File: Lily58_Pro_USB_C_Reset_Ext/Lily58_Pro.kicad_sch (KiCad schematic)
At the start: 83 parts, among them J1 LED, J2 4PIN, J3 OLED, P1 i2c_pin, P2 i2c_pin, SW1 SW_PUSH, SW2 SW_PUSH, SW3 SW_PUSH, SW4 SW_PUSH, SW5 SW_PUSH, SW6 SW_PUSH, SW7 SW_PUSH, SW8 SW_PUSH, SW9 SW_PUSH, U1 ProMicro

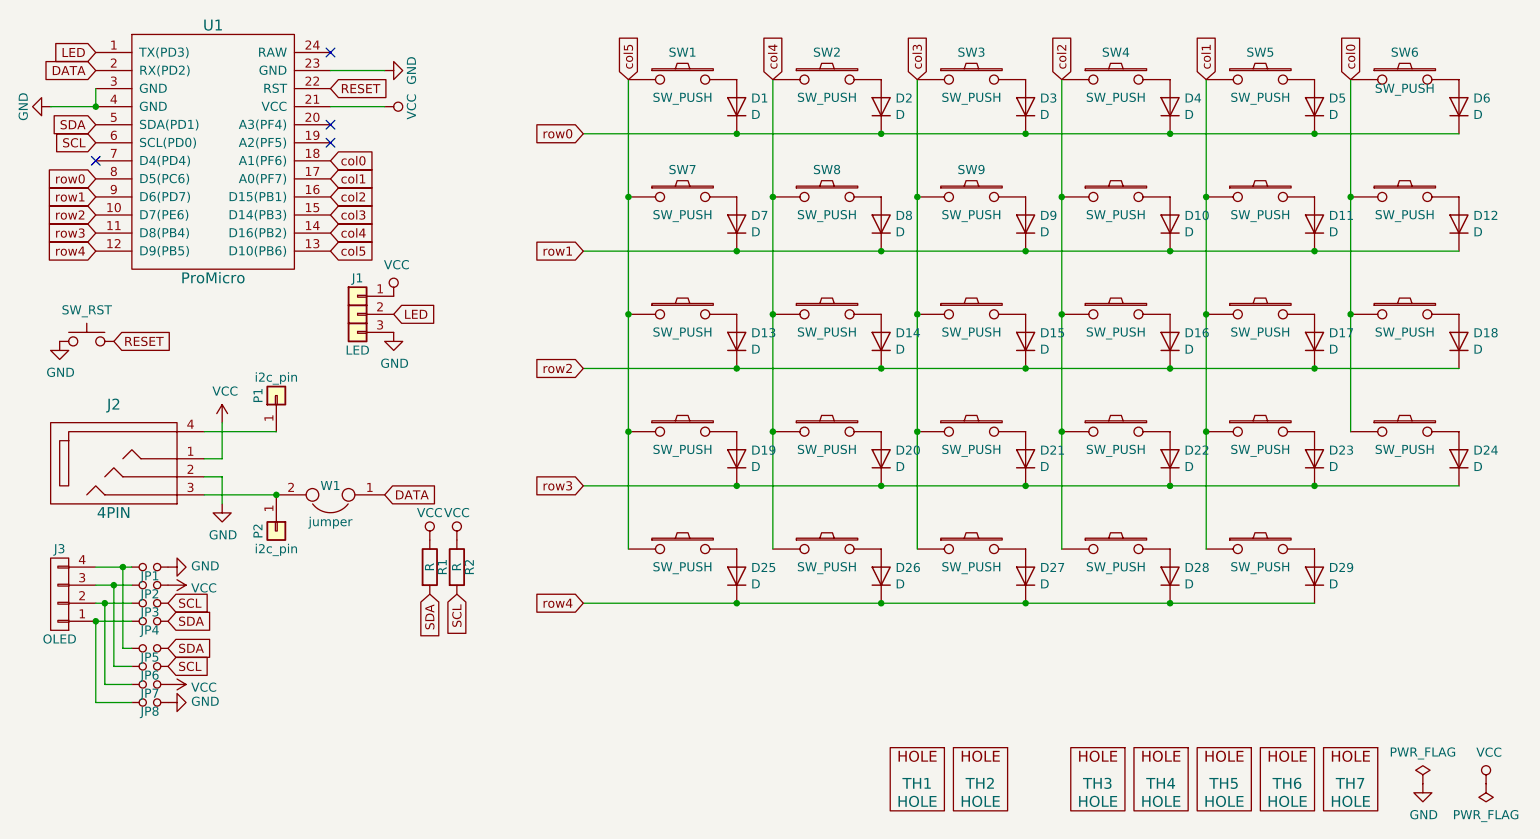
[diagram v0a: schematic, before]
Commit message: Lily58_Pro_USB_C_Reset_Ext: strip down
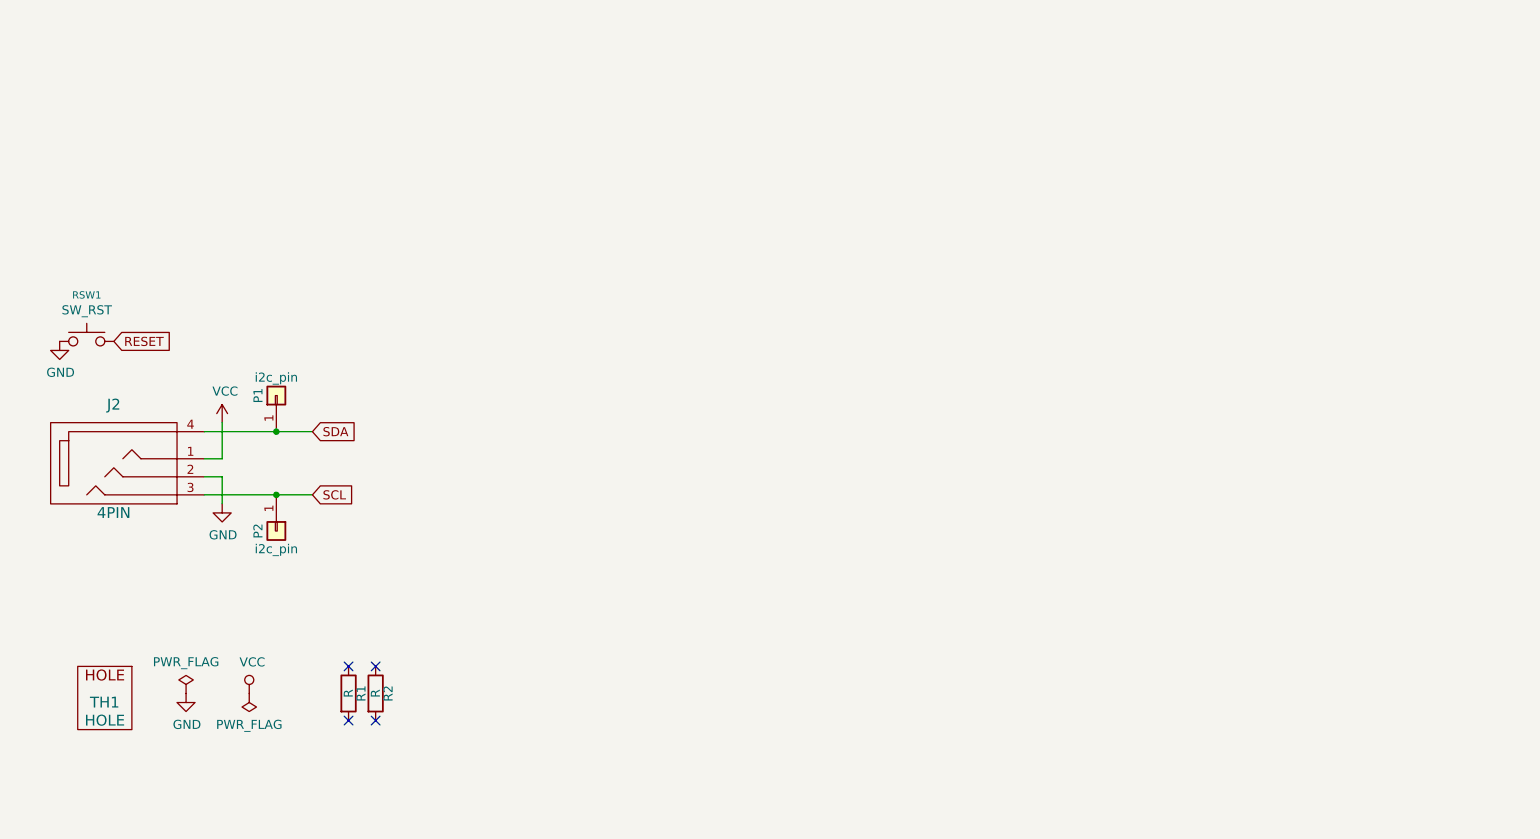
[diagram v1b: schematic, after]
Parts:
- removed ? (x20), SW1, SW2, SW3, SW4, SW5, SW6, SW7, SW8, SW9: SW_PUSH, Lily58-footprint:CherryMX_KailhLowProfile_Hotswap, symbol Lily58_Pro-rescue:SW_PUSH-Lily58-cache
- removed D1, D10, D11, D12, D13, D14, D15, D16, D17, D18, D19, D2, D20, D21, D22, D23, D24, D25, D26, D27, D28, D29, D3, D4, D5, D6, D7, D8, D9: D, Lily58-footprint:Diode_SOD123, symbol Lily58_Pro-rescue:D-Lily58-cache
- removed J1: LED, Lily58-footprint:LED, symbol Lily58_Pro-rescue:LED-Lily58-cache
- removed J3: OLED, Lily58-footprint:OLED_4Pin, symbol Lily58_Pro-rescue:OLED-Lily58-cache
- removed JP1, JP2, JP3, JP4, JP5, JP6, JP7, JP8: Jumper_NO_Small, Lily58-footprint:Jumper, symbol Lily58_Pro-rescue:Jumper_NO_Small-Device
- removed TH2: HOLE, Lily58-footprint:M2_HOLE_PCB, symbol Lily58_Pro-rescue:HOLE-Lily58-cache
- removed TH3, TH4, TH5, TH6, TH7: HOLE, Lily58-footprint:HOLE_M2_TH, symbol Lily58_Pro-rescue:HOLE-Lily58-cache
- removed U1: ProMicro, Lily58-footprint:ProMicro_rev2, symbol Lily58_Pro-rescue:ProMicro_2-Lily58-cache
- removed W1: jumper, Lily58-footprint:jumper_data, symbol Lily58_Pro-rescue:Jumper-Device
- gave numbers to parts that had none: 1
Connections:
- net SCL: now also J2.3, P2.1 (Pin_1); no longer R2.2
- net SDA: now also J2.4, P1.1 (Pin_1); no longer R1.2
- net VCC: no longer R1.1, R2.1
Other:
- moved on the sheet: R1, R2, TH1

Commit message: Lily58_Pro_USB_C_Reset_Ext: add usb and reset
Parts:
- added S1, S2: TL3330AF130QG, SW_TL3330AF130QG, symbol TL3330AF130QG:TL3330AF130QG
- added U1, U2: USB4110-GF-A_REVB, GCT_USB4110-GF-A_REVB, symbol USB4110-GF-A_REVB:USB4110-GF-A_REVB
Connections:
- net GND: now also S1.2, S2.1, U1.A1/B12 (GND), U1.B1/A12 (GND), U1.S1 (GND), U1.S2 (GND), U1.S3 (GND), U1.S4 (GND), U2.A1/B12 (GND), U2.B1/A12 (GND), U2.S1 (GND), U2.S2 (GND), U2.S3 (GND), U2.S4 (GND)
- net RESET: now also S1.1, S2.2
- net SCL: now also U1.A7 (DN1), U1.B7 (DN2), U2.A7 (DN1), U2.B7 (DN2); no longer P2.1 (Pin_1)
- net SDA: now also U1.A6 (DP1), U1.B6 (DP2), U2.A6 (DP1), U2.B6 (DP2); no longer P1.1 (Pin_1)
- net VCC: now also U1.A4/B9 (VBUS), U1.B4/A9 (VBUS), U2.A4/B9 (VBUS), U2.B4/A9 (VBUS)
- no-connect marks 4 -> 14
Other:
- moved on the sheet: P1, P2

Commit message: Lily58_Pro_USB_C_Reset_Ext: remove fill
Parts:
- S1, S2: footprint SW_TL3330AF130QG -> TL3330AF130QG:SW_TL3330AF130QG
- U1, U2: footprint GCT_USB4110-GF-A_REVB -> Usb:GCT_USB4110-GF-A_REVB
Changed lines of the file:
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@@
     (property "Reference" "U2" (id 0) (at 176.53 87.63 0))
     (property "Value" "USB4110-GF-A_REVB" (id 1) (at 176.53 90.17 0))
-    (property "Footprint" "GCT_USB4110-GF-A_REVB" (id 2) (at 176.53 102.87 0)
+    (property "Footprint" "Usb:GCT_USB4110-GF-A_REVB" (id 2) (at 176.53 102.87 0)
       (effects (font (size 1.27 1.27)) (justify left bottom) hide)
     )
@@
     (property "Reference" "S2" (id 0) (at 138.43 95.25 0))
     (property "Value" "TL3330AF130QG" (id 1) (at 138.43 97.79 0))
-    (property "Footprint" "SW_TL3330AF130QG" (id 2) (at 138.43 102.87 0)
+    (property "Footprint" "TL3330AF130QG:SW_TL3330AF130QG" (id 2) (at 138.43 102.87 0)
       (effects (font (size 1.27 1.27)) (justify left bottom) hide)
     )
@@
     (property "Reference" "S1" (id 0) (at 132.08 132.08 0))
     (property "Value" "TL3330AF130QG" (id 1) (at 132.08 134.62 0))
-    (property "Footprint" "SW_TL3330AF130QG" (id 2) (at 132.08 139.7 0)
+    (property "Footprint" "TL3330AF130QG:SW_TL3330AF130QG" (id 2) (at 132.08 139.7 0)
       (effects (font (size 1.27 1.27)) (justify left bottom) hide)
     )
@@
     (property "Reference" "U1" (id 0) (at 177.8 124.46 0))
     (property "Value" "USB4110-GF-A_REVB" (id 1) (at 177.8 127 0))
-    (property "Footprint" "GCT_USB4110-GF-A_REVB" (id 2) (at 177.8 139.7 0)
+    (property "Footprint" "Usb:GCT_USB4110-GF-A_REVB" (id 2) (at 177.8 139.7 0)
       (effects (font (size 1.27 1.27)) (justify left bottom) hide)
     )
@@
     )
     (path "/764dc4c8-395d-45d3-b5c1-398b6e9806af"
-      (reference "S1") (unit 1) (value "TL3330AF130QG") (footprint "SW_TL3330AF130QG")
+      (reference "S1") (unit 1) (value "TL3330AF130QG") (footprint "TL3330AF130QG:SW_TL3330AF130QG")
     )
     (path "/669c782c-7133-46e2-888e-a23b27c12c55"
-      (reference "S2") (unit 1) (value "TL3330AF130QG") (footprint "SW_TL3330AF130QG")
+      (reference "S2") (unit 1) (value "TL3330AF130QG") (footprint "TL3330AF130QG:SW_TL3330AF130QG")
     )
     (path "/00000000-0000-0000-0000-00005b74ce27"
@@
     )
     (path "/8d063334-2aea-4de6-9086-fa51099fd0a4"
-      (reference "U1") (unit 1) (value "USB4110-GF-A_REVB") (footprint "GCT_USB4110-GF-A_REVB")
+      (reference "U1") (unit 1) (value "USB4110-GF-A_REVB") (footprint "Usb:GCT_USB4110-GF-A_REVB")
     )
     (path "/0b41931a-e64a-4472-ae13-a1c758e836d6"
-      (reference "U2") (unit 1) (value "USB4110-GF-A_REVB") (footprint "GCT_USB4110-GF-A_REVB")
-    )
-  )
+      (reference "U2") (unit 1) (value "USB4110-GF-A_REVB") (footprint "Usb:GCT_USB4110-GF-A_REVB")
+    )
+  )
